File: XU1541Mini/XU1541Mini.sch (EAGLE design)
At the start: 18 parts, among them IC1 ATmega8, Q1 12MHz

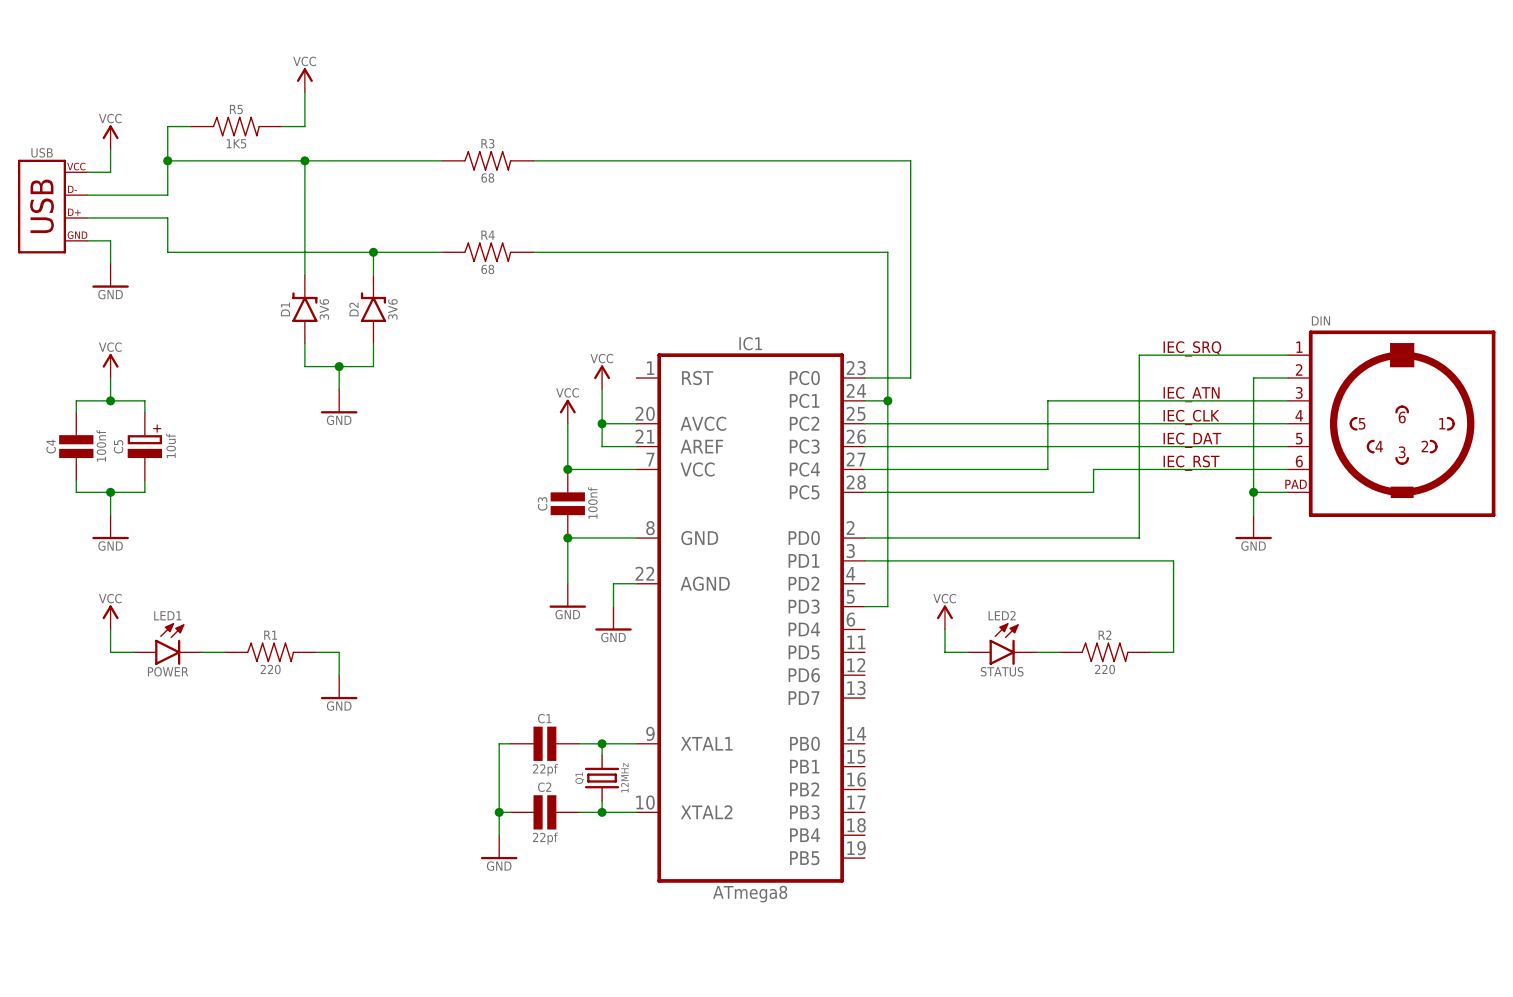
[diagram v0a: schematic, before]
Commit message: Updated project files and added missing preview images
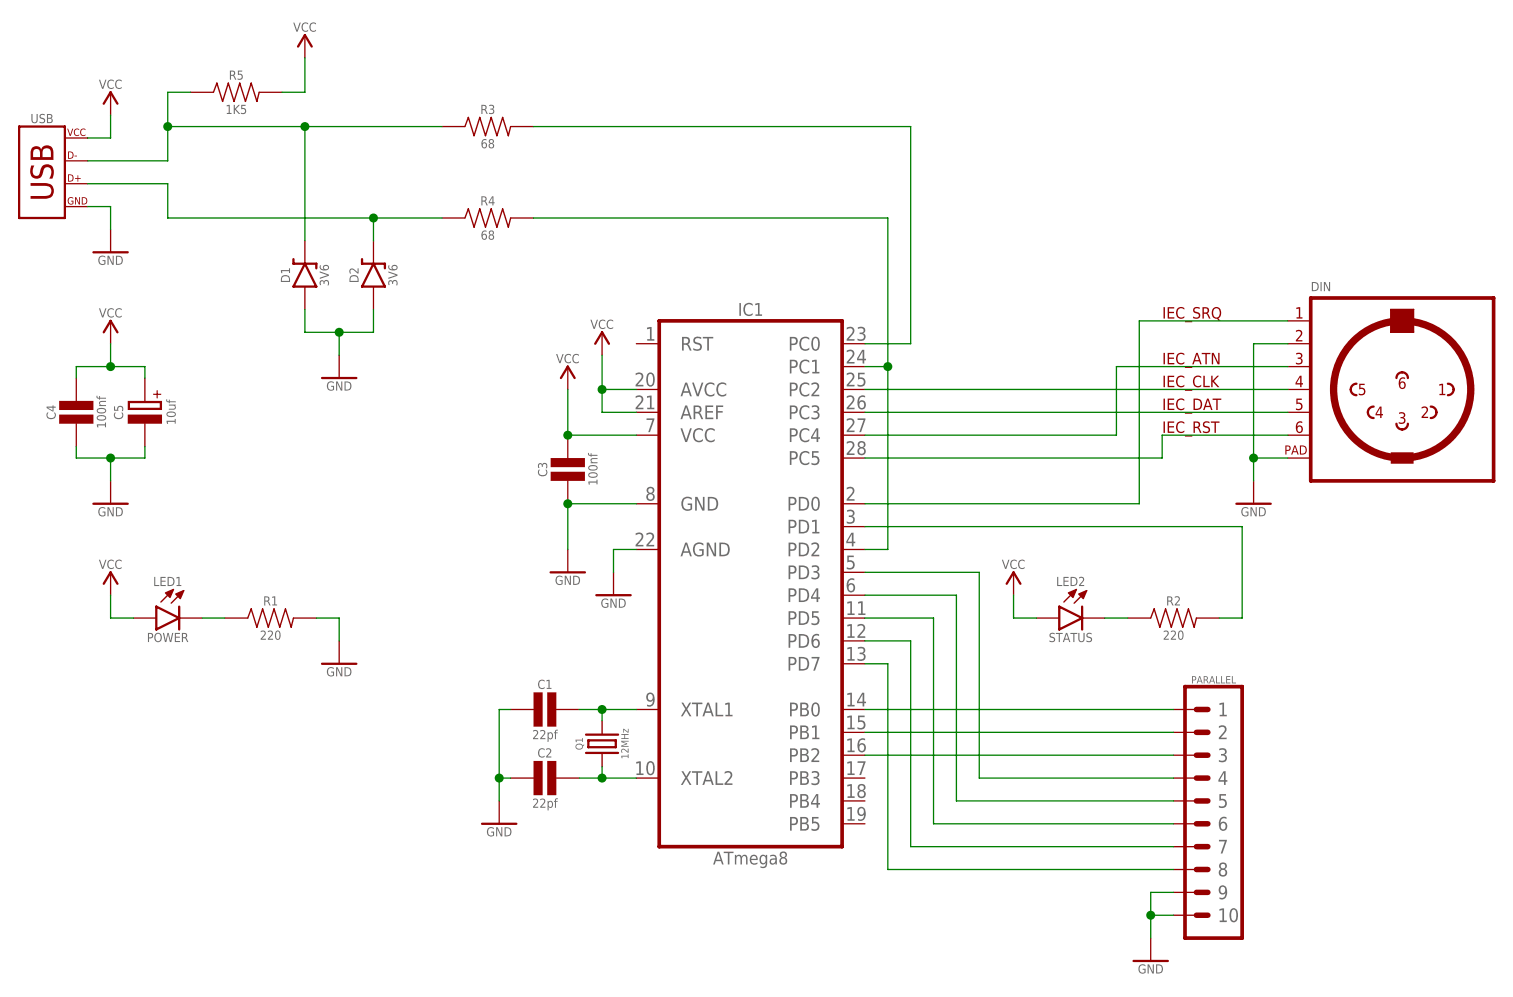
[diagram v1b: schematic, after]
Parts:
- added JP1: PARALLEL, sj_connectors:HDR_2X05
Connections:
- new net N$1: IC1.PB0, JP1.1
- new net N$2: IC1.PB1, JP1.2
- new net N$3: IC1.PB2, JP1.3
- new net N$4: IC1.PD3, JP1.4
- new net N$5: IC1.PD4, JP1.5
- new net N$6: IC1.PD5, JP1.6
- new net N$7: IC1.PD6, JP1.7
- new net N$8: IC1.PD7, JP1.8
- net D+@2: now also IC1.PD2; no longer IC1.PD3
- net GND: now also JP1.10, JP1.9
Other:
- moved on the sheet: C1, C2, C3, C4, C5, D1, D2, DIN, IC1, LED1, LED2, Q1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
